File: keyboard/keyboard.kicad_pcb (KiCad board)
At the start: 2 copper layers, 214.3 x 119.1 mm, 65 parts, among them SW1 MX_SW_HS, SW10 MX_SW_HS, SW11 MX_SW_HS, SW12 MX_SW_HS, SW13 MX_SW_HS, SW14 MX_SW_HS, SW15 MX_SW_HS, SW16 MX_SW_HS, SW17 MX_SW_HS, SW18 MX_SW_HS, SW19 MX_SW_HS, SW2 MX_SW_HS, SW20 MX_SW_HS, SW21 MX_SW_HS, SW22 MX_SW_HS, SW23 MX_SW_HS, SW24 MX_SW_HS, SW25 MX_SW_HS, SW26 MX_SW_HS, SW27 MX_SW_HS, SW28 MX_SW_HS, SW29 MX_SW_HS, SW3 MX_SW_HS, SW30 MX_SW_HS, SW31 MX_SW_HS, SW32 MX_SW_HS, SW33 MX_SW_HS, SW34 MX_SW_HS, SW35 MX_SW_HS, SW36 MX_SW_HS, SW37 MX_SW_HS, SW38 MX_SW_HS, SW39 MX_SW_HS, SW4 MX_SW_HS, SW40 MX_SW_HS, SW41 MX_SW_HS, SW42 MX_SW_HS, SW43 MX_SW_HS, SW44 MX_SW_HS, SW45 MX_SW_HS, SW46 MX_SW_HS, SW47 MX_SW_HS, SW48 MX_SW_HS, SW49 MX_SW_HS, SW5 MX_SW_HS, SW50 MX_SW_HS, SW51 MX_SW_HS, SW52 MX_SW_HS, SW53 MX_SW_HS, SW54 MX_SW_HS, SW55 MX_SW_HS, SW56 MX_SW_HS, SW57 MX_SW_HS, SW58 MX_SW_HS, SW59 MX_SW_HS, SW6 MX_SW_HS, SW60 MX_SW_HS, SW61 MX_SW_HS, SW62 MX_SW_HS, SW63 MX_SW_HS, SW64 MX_SW_HS, SW7 MX_SW_HS, SW8 MX_SW_HS, SW9 MX_SW_HS

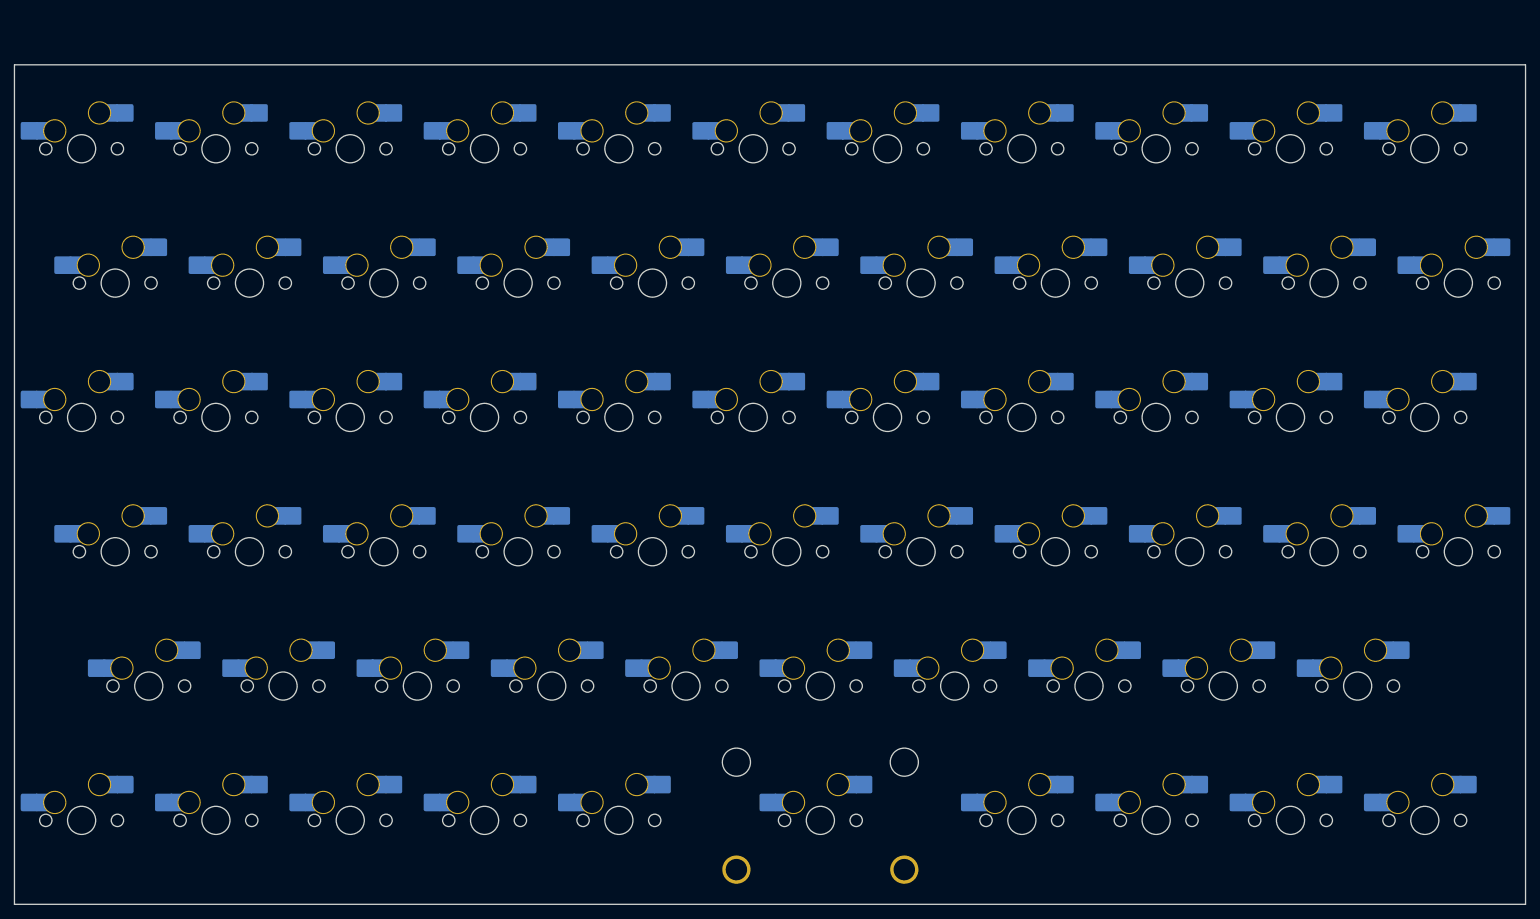
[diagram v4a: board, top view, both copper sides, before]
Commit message: Update the PCB shape
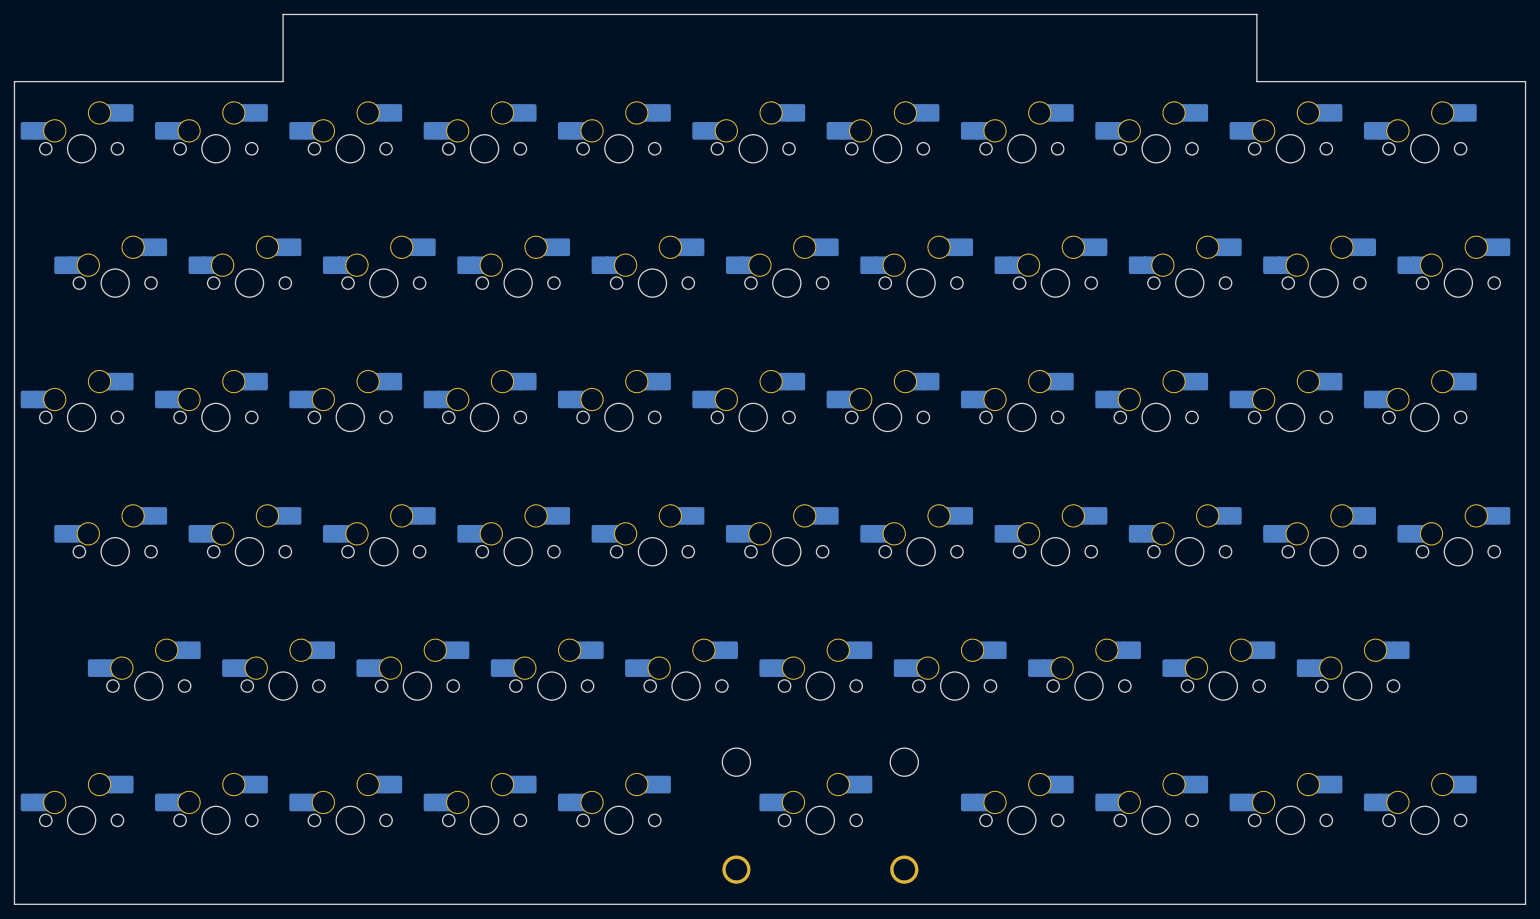
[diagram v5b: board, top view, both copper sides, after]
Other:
- board size 214.3 x 119.1 mm -> 214.3 x 126.2 mm

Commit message: Remove the top PCB lip
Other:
- board size 214.3 x 126.2 mm -> 214.3 x 133.3 mm
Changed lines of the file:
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@@
     )
   )
-  (gr_line locked (start 323.85 38.1) (end 323.85 154.78125) (layer "Edge.Cuts") (width 0.1))
-  (gr_line (start 323.85 154.78125) (end 538.1625 154.78125) (layer "Edge.Cuts") (width 0.1))
-  (gr_line (start 538.1625 154.78125) (end 538.1625 38.1) (layer "Edge.Cuts") (width 0.1))
-  (gr_line (start 500.0625 28.575) (end 361.95 28.575) (layer "Edge.Cuts") (width 0.1))
-  (gr_line (start 361.95 38.1) (end 361.95 28.575) (layer "Edge.Cuts") (width 0.1))
-  (gr_line (start 500.0625 38.1) (end 500.0625 28.575) (layer "Edge.Cuts") (width 0.1))
-  (gr_line (start 538.1625 38.1) (end 500.0625 38.1) (layer "Edge.Cuts") (width 0.1))
-  (gr_line (start 323.85 38.1) (end 361.95 38.1) (layer "Edge.Cuts") (width 0.1))
+  (gr_line (start 323.85 40.48125) (end 323.85 150.01875) (layer "Edge.Cuts") (width 0.1))
+  (gr_line (start 335.75625 171.45) (end 526.25625 171.45) (layer "Edge.Cuts") (width 0.1))
+  (gr_arc (start 330.99375 152.4) (mid 332.677548 153.097452) (end 333.375 154.78125) (layer "Edge.Cuts") (width 0.1))
+  (gr_line (start 535.78125 152.4) (end 531.01875 152.4) (layer "Edge.Cuts") (width 0.1))
+  (gr_line (start 538.1625 150.01875) (end 538.1625 40.48125) (layer "Edge.Cuts") (width 0.1))
+  (gr_arc (start 535.78125 38.1) (mid 537.465048 38.797452) (end 538.1625 40.48125) (layer "Edge.Cuts") (width 0.1))
+  (gr_arc (start 528.6375 169.06875) (mid 527.940048 170.752548) (end 526.25625 171.45) (layer "Edge.Cuts") (width 0.1))
+  (gr_line (start 333.375 154.78125) (end 333.375 169.06875) (layer "Edge.Cuts") (width 0.1))
+  (gr_line (start 326.23125 152.4) (end 330.99375 152.4) (layer "Edge.Cuts") (width 0.1))
+  (gr_arc (start 528.6375 154.78125) (mid 529.334952 153.097452) (end 531.01875 152.4) (layer "Edge.Cuts") (width 0.1))
+  (gr_arc (start 538.1625 150.01875) (mid 537.465048 151.702548) (end 535.78125 152.4) (layer "Edge.Cuts") (width 0.1))
+  (gr_line (start 528.6375 154.78125) (end 528.6375 169.06875) (layer "Edge.Cuts") (width 0.1))
+  (gr_arc (start 323.85 40.48125) (mid 324.547452 38.797452) (end 326.23125 38.1) (layer "Edge.Cuts") (width 0.1))
+  (gr_arc (start 326.23125 152.4) (mid 324.547452 151.702548) (end 323.85 150.01875) (layer "Edge.Cuts") (width 0.1))
+  (gr_arc (start 335.75625 171.45) (mid 334.072452 170.752548) (end 333.375 169.06875) (layer "Edge.Cuts") (width 0.1))
+  (gr_line (start 326.23125 38.1) (end 535.78125 38.1) (layer "Edge.Cuts") (width 0.1))
 )

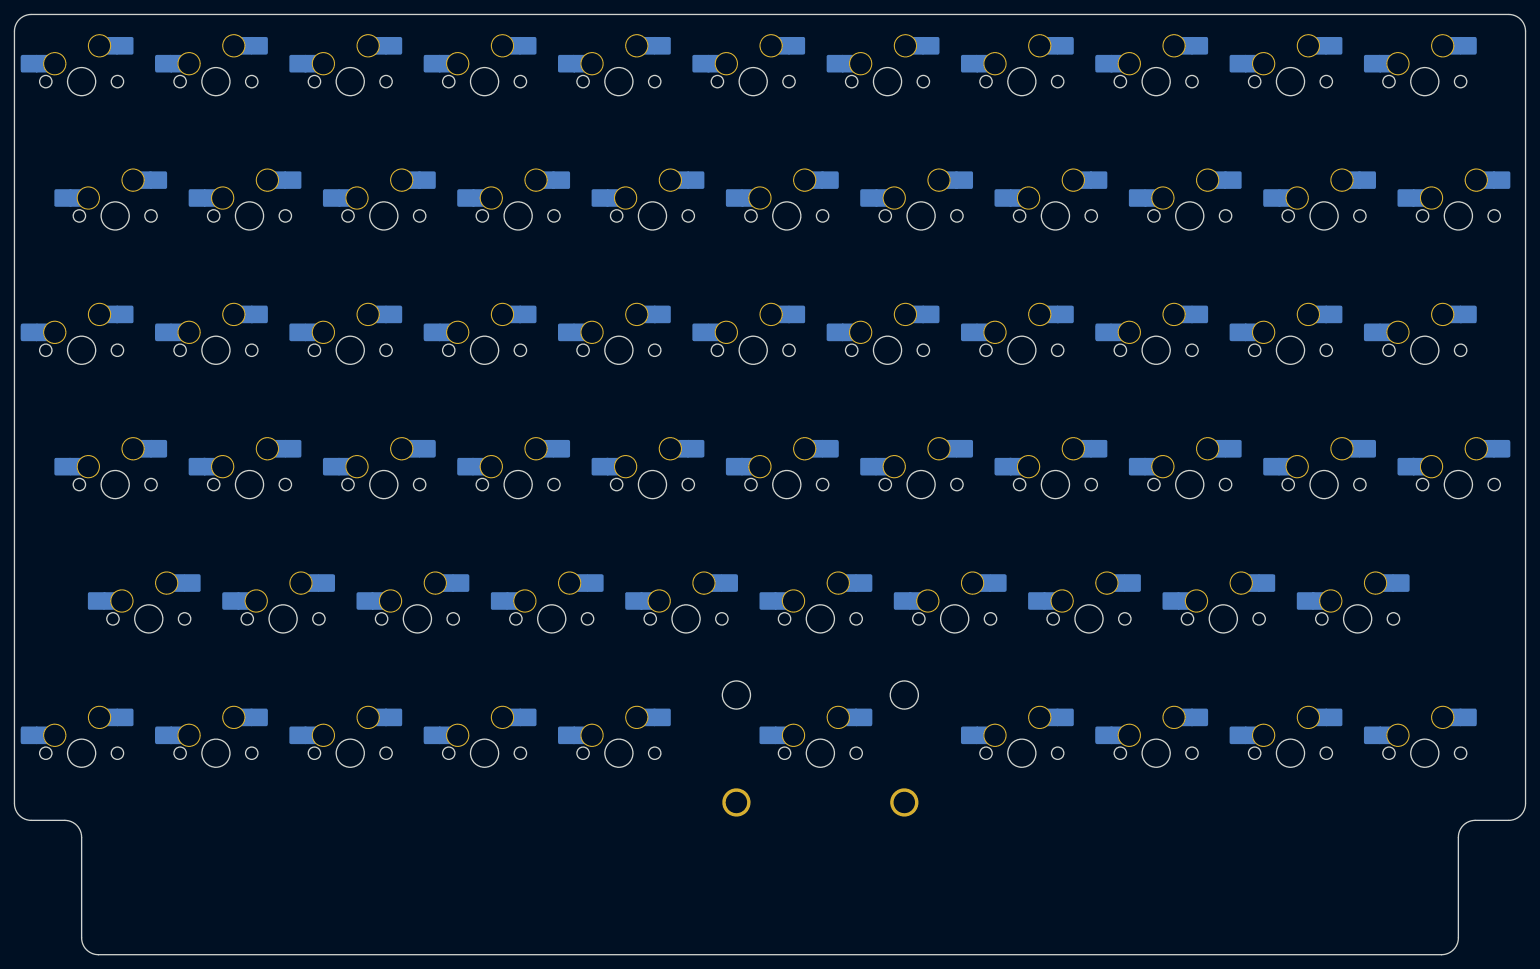
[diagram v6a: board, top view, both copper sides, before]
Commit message: Change switch orientation and shrink the board
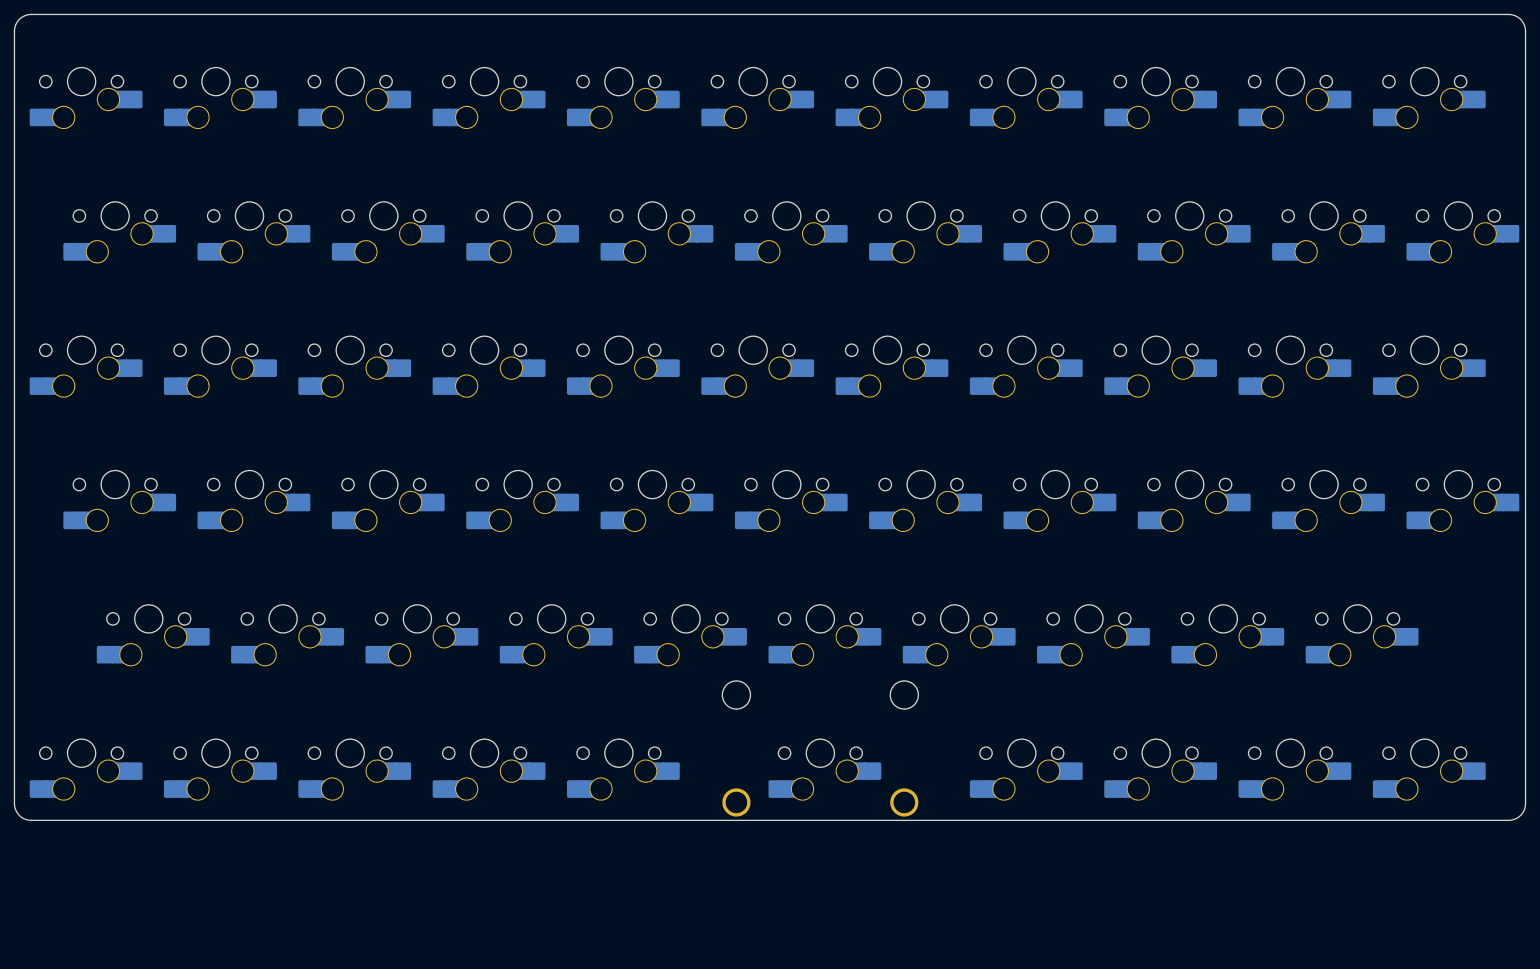
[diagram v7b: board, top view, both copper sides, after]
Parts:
- turned SW1 to 0 degrees
- turned SW10 to 0 degrees
- turned SW11 to 0 degrees
- turned SW12 to 0 degrees
- turned SW13 to 0 degrees
- turned SW14 to 0 degrees
- turned SW15 to 0 degrees
- turned SW16 to 0 degrees
- turned SW17 to 0 degrees
- turned SW18 to 0 degrees
- turned SW19 to 0 degrees
- turned SW2 to 0 degrees
- turned SW20 to 0 degrees
- turned SW21 to 0 degrees
- turned SW22 to 0 degrees
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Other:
- board size 214.3 x 133.3 mm -> 214.3 x 114.3 mm

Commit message: Add the reset switch
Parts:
- added RESET1: SW_Push, Button_Switch_THT:SW_PUSH_6mm_H13mm, F.Cu at (97.6, 33.3)
- added U1: ProMicro, Keebio-Parts:ArduinoProMicro, F.Cu at (126.2, 35.7)
- moved SW15 283.5 mm to (111.9, 73.8)
- moved SW20 283.5 mm to (207.2, 73.8)
- moved SW22 283.5 mm to (245.3, 73.8)
- moved SW25 283.5 mm to (88.1, 92.9)
- moved SW3 283.5 mm to (88.1, 54.8)
- moved SW30 283.5 mm to (183.4, 92.9)
- moved SW37 283.5 mm to (111.9, 111.9)
- moved SW42 283.5 mm to (207.2, 111.9)
- moved SW44 283.5 mm to (245.3, 111.9)
- moved SW49 283.5 mm to (135.7, 131.0)
- moved SW54 283.5 mm to (231.0, 131.0)
- moved SW57 283.5 mm to (88.1, 150.0)
- moved SW61 283.5 mm to (183.4, 150.0)
- moved SW8 283.5 mm to (183.4, 54.8)
- moved S1 283.5 mm to (154.8, 150.0)
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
